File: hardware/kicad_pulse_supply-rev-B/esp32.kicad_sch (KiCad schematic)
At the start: 29 parts, among them J1 USB_B_Micro, Q1 MMBT2222*, Q2 MMBT2222*, SW1 KMR211GLFS, U1 AP2112K-3.3, U2 ESP32-WROOM-32D, U3 CP2104

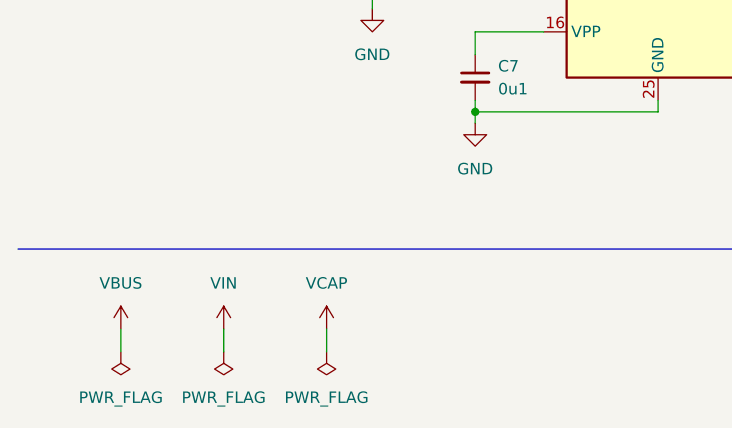
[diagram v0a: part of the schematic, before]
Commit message: Board bringup: added TPS commands
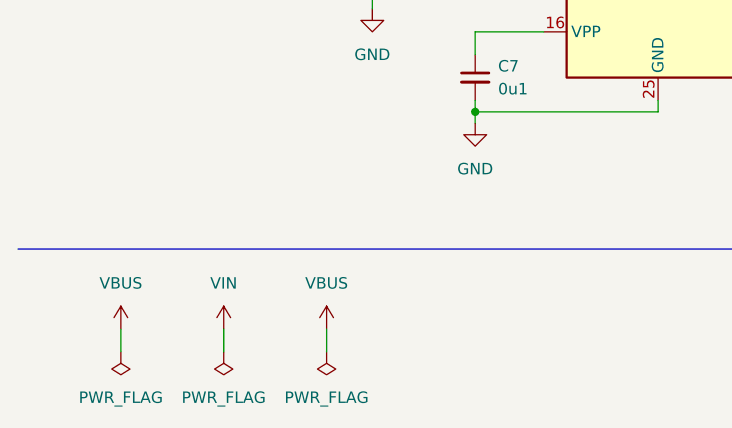
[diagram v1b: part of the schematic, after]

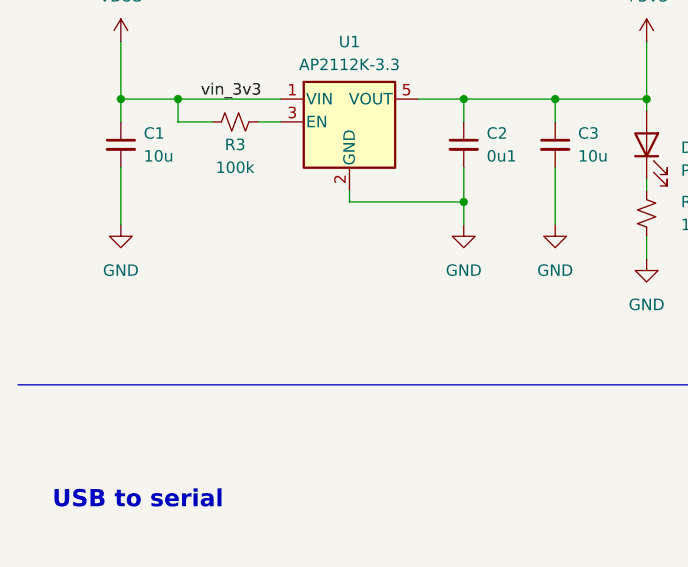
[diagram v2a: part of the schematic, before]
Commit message: Adding PCB issues to be fixed in rev C
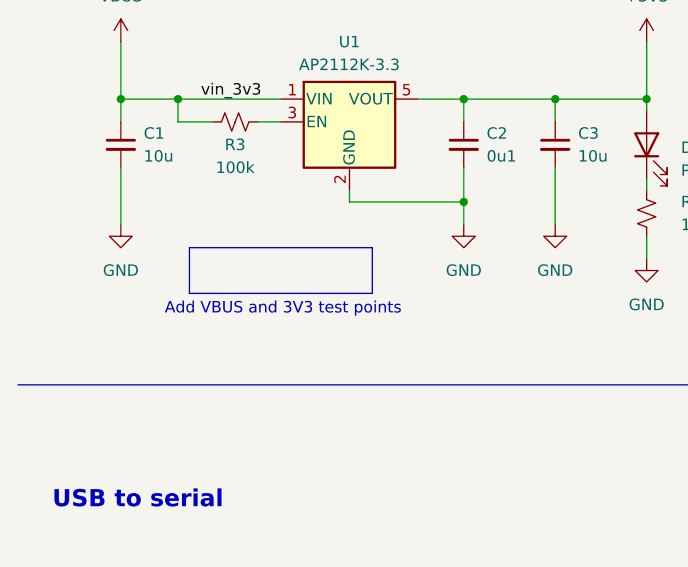
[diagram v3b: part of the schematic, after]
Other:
- note added: "Add VBUS and 3V3 test points"
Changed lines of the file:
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@@
+		)
+	)
+	(rectangle
+		(start 31.75 49.53)
+		(end 52.07 54.61)
+		(stroke
+			(width 0)
+			(type solid)
+			(color 0 0 0 1)
+		)
+		(fill
+			(type color)
+			(color 255 13 30 0.36)
+		)
+	)
+	(text "Add VBUS and 3V3 test points"
+		(exclude_from_sim no)
+		(at 42.164 56.388 0)
+		(effects
+			(font
+				(size 1.27 1.27)
+			)
 		)
 	)
